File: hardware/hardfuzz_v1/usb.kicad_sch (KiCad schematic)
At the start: 19 parts, among them J1 USB-C, U2 FT2232HQ, U3 MX25L3233F, Y2 12MHz

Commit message: hardware(kigen): review cleanup — NC flags, MPNs, PG/flag fixes, FPGA on A1
Address kicad-happy skill + ERC findings on the hierarchical board:
- no-connect flags on all intentional spare pins (unconnected 238 -> 0)
- MPNs on 16 ICs/connectors; grid-snapped endpoints
- fix buck PG mis-map (was tied to VIN) and drop double-driver PWR_FLAGs
- rename FT core rail VDDCORE_FT so PP-001 reads it as an internal rail (info)
- FPGA sub-sheet on A1 so all 5 units fit on the page
kigen gains no_connect + MPN emission. Skill review now: 1 error (SS-001
sourcing gate, needs passive MPNs) + benign info; netlist connectivity intact.

Co-Authored-By: Claude Opus 4.8 <noreply@anthropic.com>
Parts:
- D30: MPN (none) -> USBLC6-2SC6
- J1: MPN (none) -> USB4085-GF-A
- U2: MPN (none) -> FT2232HQ-REEL
- U3: MPN (none) -> MX25L3233FM2I-08G
- Y2: MPN (none) -> ABM8-12.000MHZ-B2-T
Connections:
- net FT_1V8 renamed VDDCORE_FT
- no-connect marks 0 -> 41

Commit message: hardware: generate placed PCB (hardfuzz_v1.kicad_pcb) + footprints; rename root
kigen_pcb.py generates the PCB from the schematic netlist: loads each part's
stock .kicad_mod, shelf-packs footprints (origin-offset so courtyards don't
overlap), injects pad nets, and adds a board outline + 2-layer stackup. Loads in
pcbnew with 68 footprints and 302 nets on the right pads; the 317 'unconnected'
are the unrouted nets (routing is interactive/autorouter — the generator sets it
up, doesn't draw copper).

Also: assigned real footprints to the 6 ICs that lacked them and fixed 2 wrong
names (all now resolve, incl BGA-324 + QFN-64). Renamed the root schematic/PCB to
hardfuzz_v1.* so the project opens linked as hardfuzz_v1.kicad_pro.

Co-Authored-By: Claude Opus 4.8 <noreply@anthropic.com>
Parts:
- U2: footprint (none) -> Package_DFN_QFN:QFN-64-1EP_9x9mm_P0.5mm_EP4.35x4.35mm
- U3: footprint Package_SO:SOIC-8_5.23x5.23mm_P1.27mm -> Package_SO:SOIC-8_3.9x4.9mm_P1.27mm

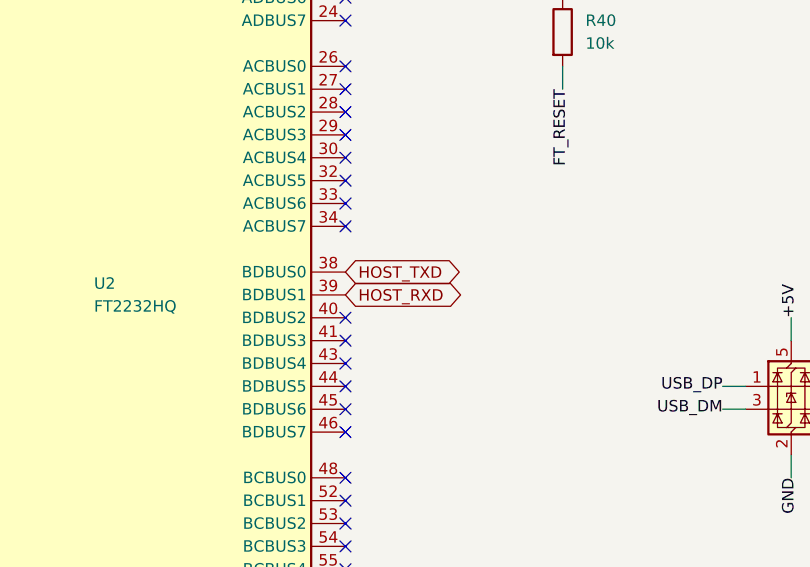
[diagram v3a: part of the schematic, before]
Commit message: v2: standalone/BLE architecture doc + ESP32 controller added to the board
docs/HardFuzz_v2_Standalone.md: computer-free architecture — an on-board ESP32-S3
runs the header-only C++ campaign engine (ports nearly as-is), arms the FPGA over
UART, drives the DUT, and streams results to a phone app over BLE. Includes the GATT
service definition and the host-engine -> ESP32 mapping.

Design: gen/esp32_sheet.py adds the ESP32-S3-WROOM-1 (power, EN/IO0 boot circuits,
UART to FPGA via the freed FT2232 ch-B control nets, UART to a DUT header, USB-C for
programming, BLE LED). Regenerated schematic (7 sheets, 83 parts) + PCB (loads,
ESP32 placed). FT2232 keeps JTAG; ESP32 owns the runtime control path.

Co-Authored-By: Claude Opus 4.8 <noreply@anthropic.com>
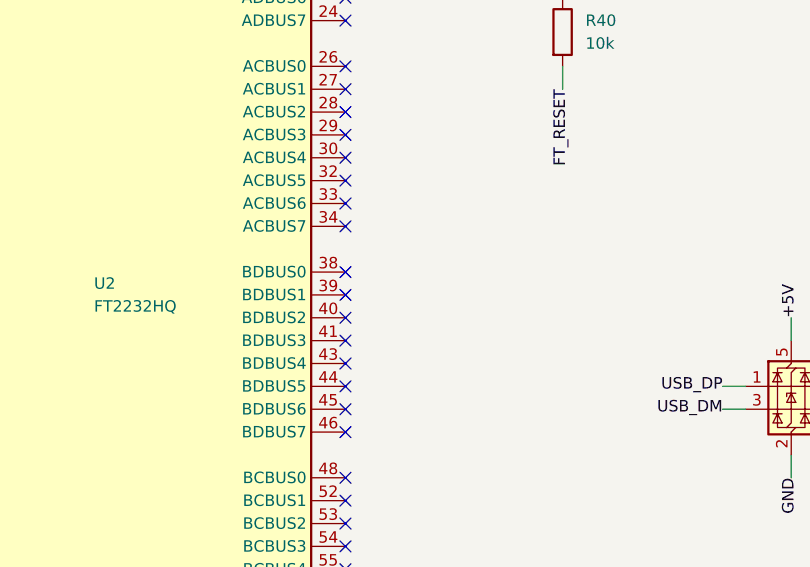
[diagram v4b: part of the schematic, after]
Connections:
- net HOST_RXD: no longer names the net of U2.39 (BDBUS1)
- net HOST_TXD: no longer names the net of U2.38 (BDBUS0)
- no-connect marks 41 -> 43
